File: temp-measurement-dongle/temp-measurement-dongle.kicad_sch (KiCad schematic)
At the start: 41 parts, among them J1 1.47 IPS LCD, J2 USB2UART, Q1 SS8050, Q2 SS8050, SW1 RST, SW2 Boot, SW3 IN1, SW4 IN2, SW5 IN4, SW6 IN4, U1 ESP32-S3-WROOM-1, U2 CH340C, U4 AMS1117-3.3

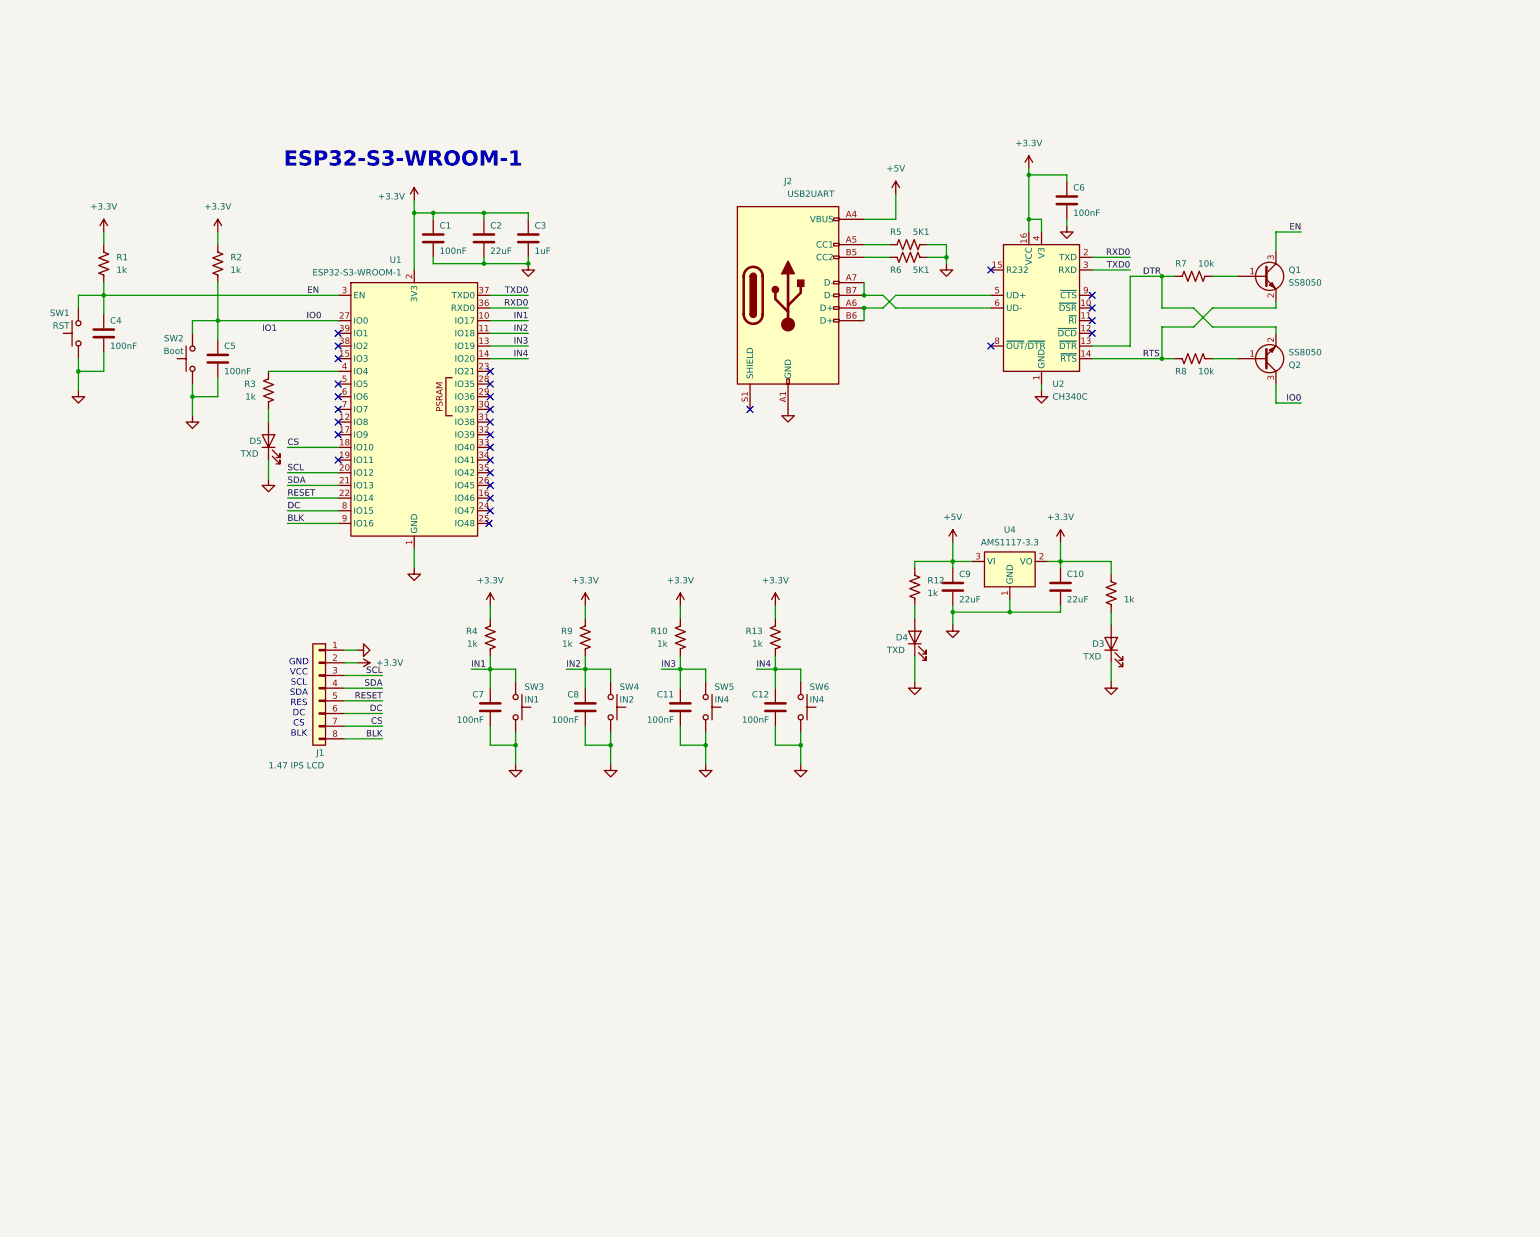
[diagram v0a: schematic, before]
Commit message: feat: finish schematic of temperature-measurement-dongle
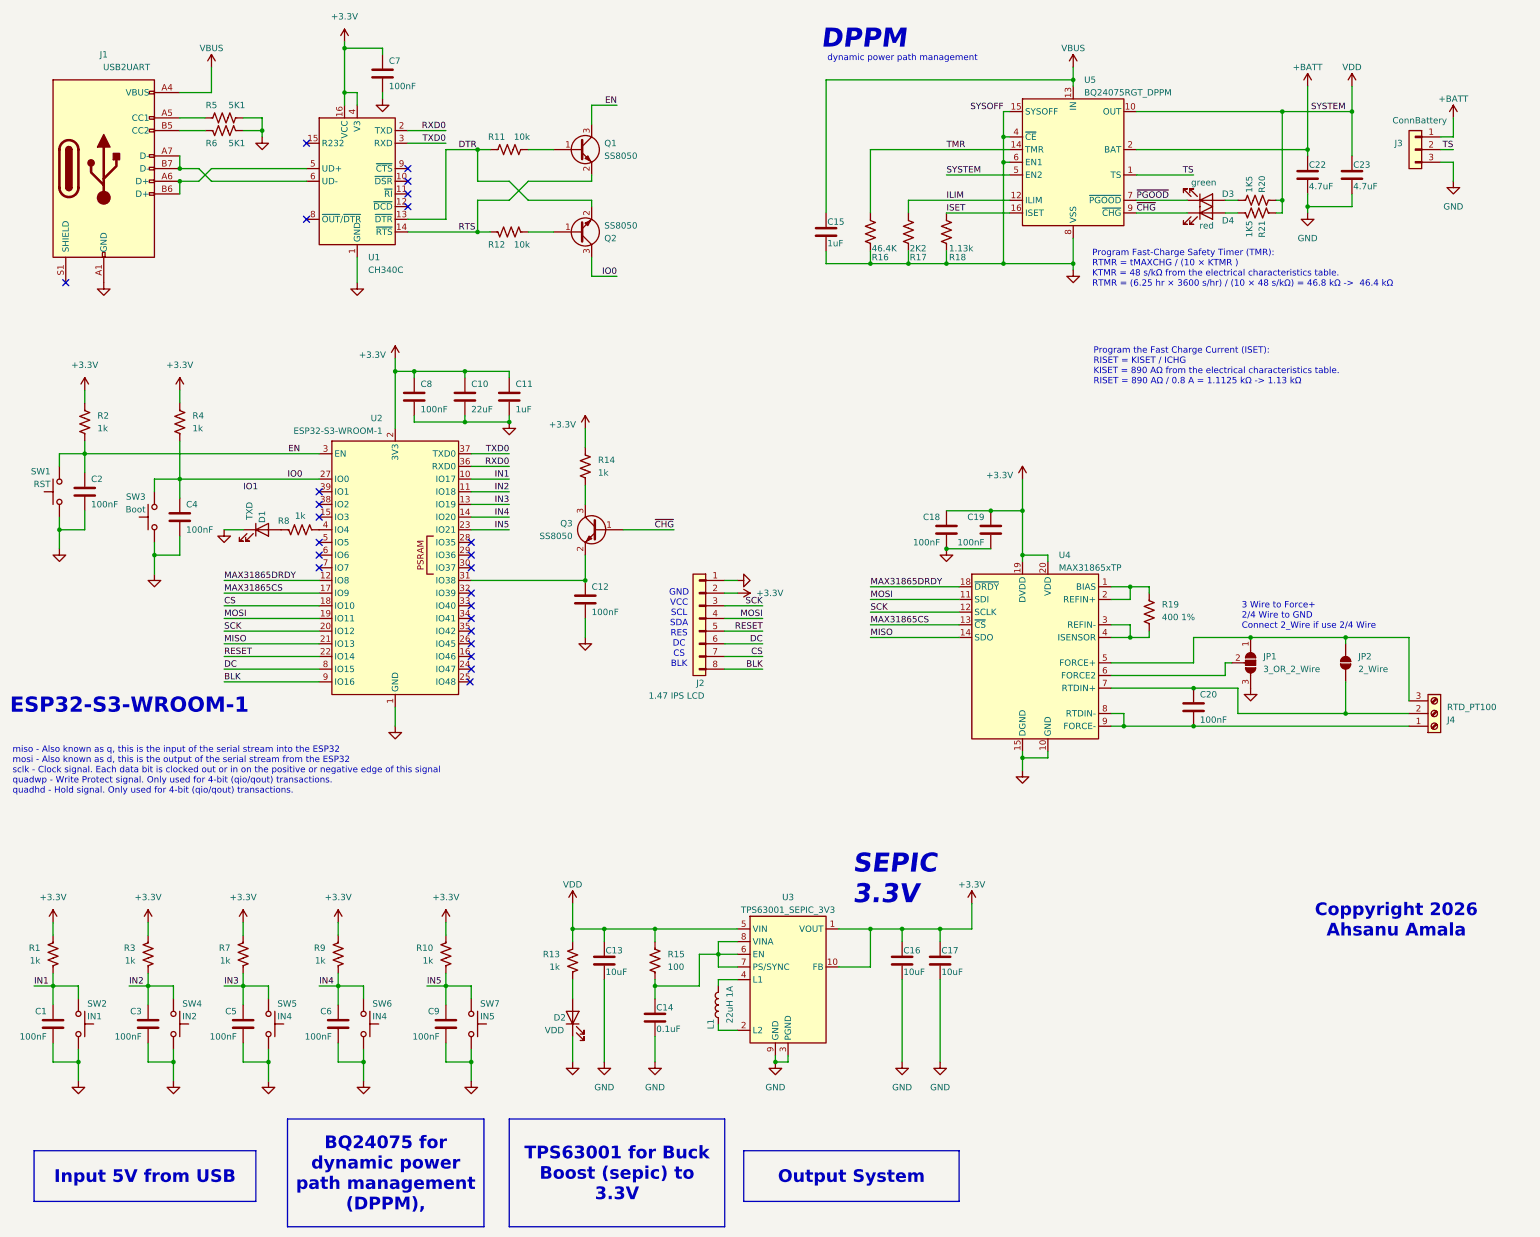
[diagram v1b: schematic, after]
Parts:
- removed C10: 22uF, Capacitor_SMD:C_0805_2012Metric_Pad1.18x1.45mm_HandSolder, symbol Device:C
- removed R11: 1k, Resistor_SMD:R_0805_2012Metric_Pad1.20x1.40mm_HandSolder, symbol Device:R_US
- removed U4: AMS1117-3.3, Package_TO_SOT_SMD:SOT-223-3_TabPin2, symbol Regulator_Linear:AMS1117-3.3
- added C12, C18, C19, C20: 100nF, Capacitor_SMD:C_0805_2012Metric_Pad1.18x1.45mm_HandSolder, symbol Device:C
- added C13, C16, C17: 10uF, Capacitor_SMD:C_0805_2012Metric_Pad1.18x1.45mm_HandSolder, symbol Device:C
- added C14: 0.1uF, Capacitor_SMD:C_0805_2012Metric_Pad1.18x1.45mm_HandSolder, symbol Device:C
- added C15: 1uF, Capacitor_SMD:C_0805_2012Metric_Pad1.18x1.45mm_HandSolder, symbol Device:C
- added C22, C23: 4.7uF, Capacitor_SMD:C_0805_2012Metric_Pad1.18x1.45mm_HandSolder, symbol Device:C
- added D4: red, LED_SMD:LED_0805_2012Metric_Pad1.15x1.40mm_HandSolder, symbol Device:LED
- added J3: ConnBattery, Connector_PinHeader_2.54mm:PinHeader_1x03_P2.54mm_Vertical, symbol Connector_Generic:Conn_01x03
- added J4: RTD_PT100, TerminalBlock_Phoenix:TerminalBlock_Phoenix_PT-1,5-3-5.0-H_1x03_P5.00mm_Horizontal, symbol Connector:Screw_Terminal_01x03
- added JP1: 3_OR_2_Wire, Jumper:SolderJumper-3_P1.3mm_Open_RoundedPad1.0x1.5mm, symbol Jumper:SolderJumper_3_Open
- added JP2: 2_Wire, Jumper:SolderJumper-2_P1.3mm_Open_TrianglePad1.0x1.5mm, symbol Jumper:SolderJumper_2_Open
- added L1: 22uH 1A, Inductor_SMD:L_Bourns_SRP7028A_7.3x6.6mm, symbol Device:L
- added Q3: SS8050, Package_TO_SOT_SMD:SOT-23_Handsoldering, symbol Transistor_BJT:BC817
- added R10, R14: 1k, Resistor_SMD:R_0805_2012Metric_Pad1.20x1.40mm_HandSolder, symbol Device:R_US
- added R15: 100, Resistor_SMD:R_0805_2012Metric_Pad1.20x1.40mm_HandSolder, symbol Device:R_US
- added R16: 46.4K, Resistor_SMD:R_0805_2012Metric_Pad1.20x1.40mm_HandSolder, symbol Device:R_US
- added R17: 2K2, Resistor_SMD:R_0805_2012Metric_Pad1.20x1.40mm_HandSolder, symbol Device:R_US
- added R18: 1.13k, Resistor_SMD:R_0805_2012Metric_Pad1.20x1.40mm_HandSolder, symbol Device:R_US
- added R19: 400 1%, Resistor_SMD:R_0805_2012Metric_Pad1.20x1.40mm_HandSolder, symbol Device:R_US
- added R20, R21: 1K5, Resistor_SMD:R_0805_2012Metric_Pad1.20x1.40mm_HandSolder, symbol Device:R_US
- added SW7: IN5, Button_Switch_SMD:SW_SPST_PTS810, symbol Switch:SW_Push
- added U3: TPS63001_SEPIC_3V3, Package_SON:Texas_DRC0010J_ThermalVias, symbol Regulator_Switching:TPS63001
- added U4: MAX31865xTP, Package_DFN_QFN:TQFN-20-1EP_5x5mm_P0.65mm_EP3.25x3.25mm, symbol Sensor_Temperature:MAX31865xTP
- added U5: BQ24075RGT_DPPM, Package_DFN_QFN:VQFN-16-1EP_3x3mm_P0.5mm_EP1.6x1.6mm, symbol Battery_Management:BQ24075RGT
- C9: value 22uF -> 100nF
- D2: renamed from D4; value TXD -> VDD
- D3: value TXD -> green; footprint LED_SMD:LED_1206_3216Metric_Pad1.42x1.75mm_HandSolder -> LED_SMD:LED_0805_2012Metric_Pad1.15x1.40mm_HandSolder
- renumbered C7 to C1, C2 to C10, C3 to C11, C4 to C2, C8 to C3, C5 to C4, C11 to C5, C12 to C6, C6 to C7, C1 to C8, D5 to D1, J2 to J1, J1 to J2, R4 to R1, R7 to R11, R8 to R12, R12 to R13, R1 to R2, R9 to R3, R2 to R4, R10 to R7, R3 to R8, R13 to R9, SW3 to SW2, SW2 to SW3, U2 to U1, U1 to U2
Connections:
- net +3.3V: now also C16.1, C17.1, C18.1, C19.1, R10.1, R14.1, U3.1 (VOUT), U3.10 (FB), U4.19 (DVDD), U4.20 (VDD)
- net GND: now also C12.2, C13.2, C14.2, C15.2, C16.2, C17.2, C18.2, C19.2, C22.2, C23.2, J3.3 (Pin_3), JP1.3 (B), R16.2, R17.2, R18.2, SW7.1, U3.11 (PGND), U3.3 (PGND), U3.9 (GND), U4.10 (GND), U4.15 (DGND), U4.16 (GND), U4.21 (GND), U5.15 (SYSOFF), U5.17 (VSS), U5.4 (~{CE}), U5.6 (EN1), U5.8 (VSS); no longer D3.1 (K)
- net at D3.2 (A): now also R20.1
- net at R8.1: now also D1.2 (A); no longer U2.4 (IO4)
- net at R8.2: now also U2.4 (IO4); no longer D1.2 (A)
- net MAX31865DRDY: now reaches U2.12 (IO8)
- net MAX31865DRDY: now also U4.18 (~{DRDY})
- net MAX31865CS: now reaches U2.17 (IO9)
- net MAX31865CS: now also U4.13 (~{CS})
- net MOSI: now reaches U2.19 (IO11)
- net MOSI: now also J2.4 (Pin_4), U4.11 (SDI)
- net IN5: now reaches U2.23 (IO21)
- net IN5: now also C9.1, R10.2, SW7.2
- net at U2.31 (IO38): now also C12.1, Q3.2 (E)
- net +5V renamed VBUS
- net VBUS: now also C15.1, U5.13 (IN); no longer C9.1, R13.1
- net SCL renamed SCK
- net SCK: now also U4.12 (SCLK)
- net SDA renamed MISO
- net MISO: now also U4.14 (SDO); no longer J2.4 (Pin_4)
- new net: L1.1, U3.2 (L2)
- new net: L1.2, U3.4 (L1)
- new net: Q3.3 (C), R14.2
- new net: C20.2, J4.1 (Pin_1), U4.8 (RTDIN-), U4.9 (FORCE-)
- new net: C20.1, J4.2 (Pin_2), JP2.1 (A), U4.7 (RTDIN+)
- new net: J4.3 (Pin_3), JP1.1 (A), JP2.2 (B), U4.5 (FORCE+)
- new net: R19.1, U4.1 (BIAS), U4.2 (REFIN+)
- new net: R19.2, U4.3 (REFIN-), U4.4 (ISENSOR)
- new net: JP1.2 (C), U4.6 (FORCE2)
- new net: C14.1, R15.2, U3.6 (EN), U3.7 (PS/SYNC), U3.8 (VINA)
- new net: D4.2 (A), R21.1
- new net +BATT: C22.1, J3.1 (Pin_1), U5.2 (BAT), U5.3 (BAT)
- new net ILIM: R17.1, U5.12 (ILIM)
- new net ISET: R18.1, U5.16 (ISET)
- new net TMR: R16.1, U5.14 (TMR)
- new net TS: J3.2 (Pin_2), U5.1 (TS)
- new net VDD: C13.1, C23.1, R13.1, R15.1, R20.2, R21.2, U3.5 (VIN), U5.10 (OUT), U5.11 (OUT), U5.5 (EN2)
- new net ~{CHG}: D4.1 (K), Q3.1 (B), U5.9 (~{CHG})
- new net ~{PGOOD}: D3.1 (K), U5.7 (~{PGOOD})
- no-connect marks 29 -> 24
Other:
- note added: "3 Wire to Force+ 2/4 Wire to GND Connect 2_Wire if use 2/4 Wire"
- note added: "DPPM"
- note added: "Program Fast-Charge Safety Timer (TMR): RTMR = tMAXCHG / (10 × KTMR ) KTMR = 48 s/kΩ from the electrical characteristics table. RTMR = (6.25 hr × 3600 s/hr) / (10 × 48 s/kΩ) = 46.8 kΩ -> 46.4 kΩ"
- note added: "Program the Fast Charge Current (ISET): RISET = KISET / ICHG KISET = 890 AΩ from the electrical characteristics table. RISET = 890 AΩ / 0.8 A = 1.1125 kΩ -> 1.13 kΩ"
- note added: "SEPIC 3.3V"
- note added: "dynamic power path management"
- note added: "miso - Also known as q, this is the input of the serial stream into the ESP32 mosi - Also known as d, this is the output of the serial stream from the ESP32 sclk - Clock signal. Each data bit is clocked out or in on the positive or negative edge of this signal quadwp - Write Protect signal. Only used for 4-bit (qio/qout) transactions. quadhd - Hold signal. Only used for 4-bit (qio/qout) transacti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"
- title: Prototype Double Layer -> Temperature Measurement Dongle
- moved on the sheet: C1, C10, C11, C2, C3, C4, C5, C6, C7, C8, D1, D2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

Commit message: feat: finish 2 layer routing temperature measurement dongle
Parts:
- added H1, H2, H3, H4: MountingHole, MountingHole:MountingHole_2mm, symbol Mechanical:MountingHole
- D1: value TXD -> INDICATOR
- SW2, SW4, SW5, SW6, SW7: footprint Button_Switch_SMD:SW_SPST_PTS810 -> Button_Switch_SMD:SW_SPST_Omron_B3FS-100xP
